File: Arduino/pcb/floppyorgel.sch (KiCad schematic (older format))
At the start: 31 parts, among them J1 Floppy-Bus, J2 Floppy-Bus, J3 FTDI, J4 Buck-Converter-5V, J5 MAX485 Socket, J6 Buck-Converter-12V, J7 IBM_PC_Floppy_IDC, J8 Power Select, J9 Floppy-Power, SW1 Bus Address Select, SW2 Reset Button, U1 ATMEGA328P-AU, U2 74HC595, Y1 20 Mhz Crystal

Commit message: floppyorgel.sch: add bypass caps
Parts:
- added C? (x4): 100nF, symbol Device:C
- added C?: 1500uF, symbol Device:CP
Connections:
- net labels added: LATCH_ADDR, LATCH_LED
- wire segments 169 -> 182
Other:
- note added: "Bypass"
- moved on the sheet: D?, R?, SW1, U2, U?

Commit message: floppyorgel.sch: add hierachical sheets
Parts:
- gave numbers to parts that had none: 22

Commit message: floppyorgel.sch: reduce ERC errors
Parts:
- added R9: 4K7, symbol Device:R
- renumbered J3 to J1, J1 to J2, J4 to J3, J5 to J4, J2 to J5, J8 to J7, J9 to J8, J7 to J9, R9 to R10, R10 to R11, R11 to R12, R12 to R13, SW2 to SW1, SW1 to SW2
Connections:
- net labels removed: +24V, nLATCH
- wire segments 182 -> 185
- no-connect marks 24 -> 35

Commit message: pcb: continue wiring / move parts to hierachival sheets
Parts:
- removed C1, C3, C4, C5, C6: 100nF, symbol Device:C
- removed C2: 1500uF, symbol Device:CP
- removed C7, C8: 22pF, symbol Device:C
- removed D1: LED_RGB, symbol Device:LED_RGB
- removed J1: FTDI, Connector_PinHeader_2.54mm:PinHeader_1x06_P2.54mm_Vertical, symbol ftdi:FTDI
- removed J2, J5: Floppy-Bus, shrouded:Shrouded_Header_2x05_Pitch2.54mm, symbol floppy-bus-connector:Floppy-Bus
- removed J3: Buck-Converter-5V, Connector_PinHeader_2.54mm:PinHeader_1x06_P2.54mm_Vertical, symbol buck-converter:Buck-Converter
- removed J4: MAX485 Socket, Housings_DIP:DIP-8_W7.62mm, symbol Interface_UART:MAX485E
- removed J6: Buck-Converter-12V, Connector_PinHeader_2.54mm:PinHeader_1x06_P2.54mm_Vertical, symbol buck-converter:Buck-Converter
- removed J7: Power Select, Pin_Headers:Pin_Header_Straight_1x02_Pitch2.54mm, symbol Connector:Conn_01x03_Male
- removed J8: Floppy-Power, floppy_power:Floppy_Power_1x04_Pitch2.54mm, symbol floppy-power:Floppy-Power
- removed J9: IBM_PC_Floppy_IDC, Connector_PinHeader_2.54mm:PinHeader_2x17_P2.54mm_Horizontal, symbol ibm_pc_floppy_idc:IBM_PC_Floppy_IDC
- removed R1: 10K, symbol Device:R
- removed R10, R11, R12, R13, R2, R3, R4, R5, R6, R7, R8, R9: 4K7, symbol Device:R
- removed SW1: Reset Button, Buttons_Switches_THT:SW_PUSH_6mm, symbol floppyorgel-rescue:SW_Push_Dual-RESCUE-floppyorgel
- removed SW2: Bus Address Select, Buttons_Switches_THT:SW_DIP_x6_W7.62mm_Slide, symbol floppyorgel-rescue:SW_DIP_x06-switches
- removed U1: ATMEGA328P-AU, Housings_QFP:TQFP-32_7x7mm_Pitch0.8mm, symbol floppyorgel-rescue:ATMEGA328P-AU-atmel
- removed U2: 74HC595, SMD_Packages:SO-16-N, symbol floppyorgel-rescue:74HC595-74xx
- removed U3: 4021, symbol 4xxx_IEEE:4021
- removed Y1: 20 Mhz Crystal, Crystals:Crystal_HC49-4H_Vertical, symbol floppyorgel-rescue:Crystal-device
- added J1: VCC_Power_Select, symbol vcc_power_select:VCC_Power_Select
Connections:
- net labels added: 12V_BUS, 5V_BUS, 5V_ISP
- net labels removed: BUS_POWER, BUS_RX, BUS_TX, DIRECTION, DRIVE_SELECT, GND, LATCH_ADDR, LATCH_LED, MISO, MOSI, RESET, SCK, STEP, TRK00, VCC_BUS, VCC_ISP
- wire segments 185 -> 24
- no-connect marks 35 -> 0
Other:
- note removed: "Bypass"
- note removed: "Output to next module"

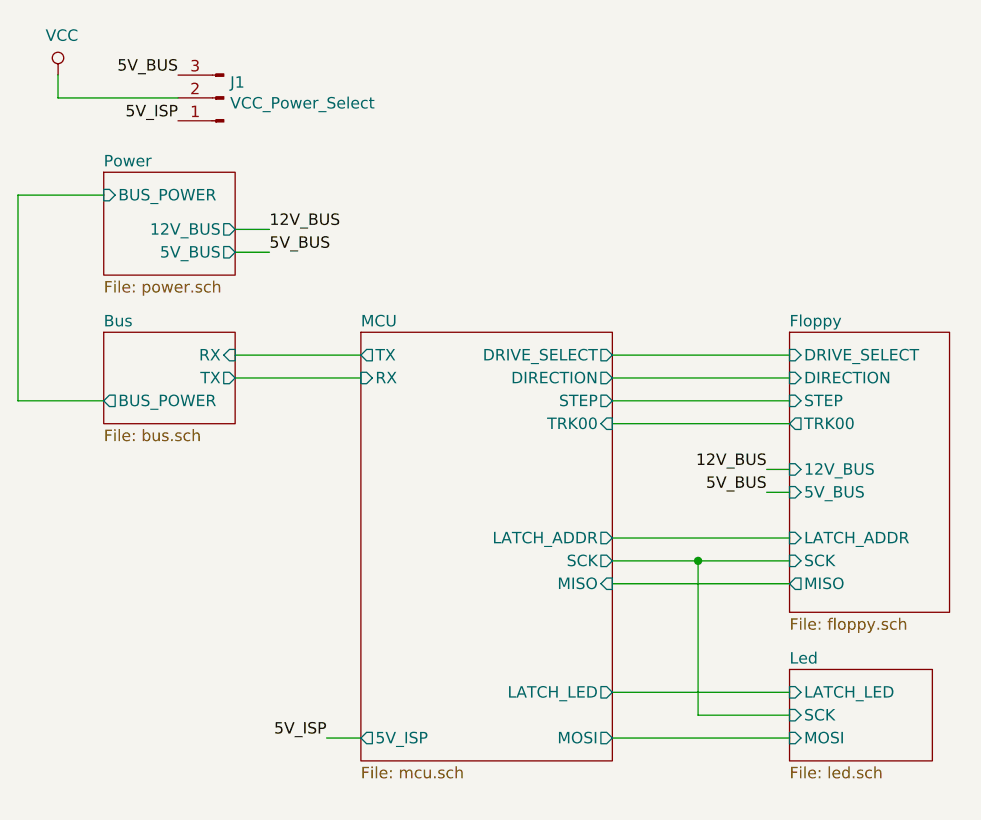
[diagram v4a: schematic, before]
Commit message: pcb: finish wiring / use ws2812 under chip led
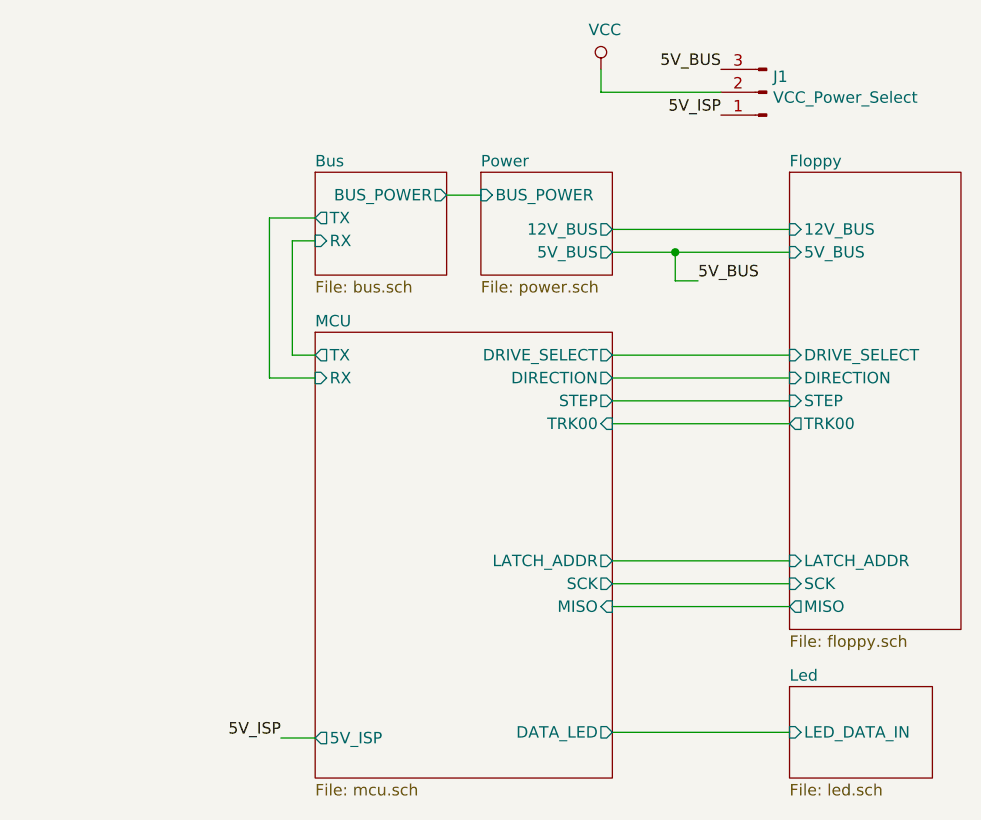
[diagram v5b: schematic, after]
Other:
- moved on the sheet: J1
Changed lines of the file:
@@
 $EndDescr
 $Sheet
-S 5800 3475 700  1225
+S 3725 2775 575  450
+U 5CD1E0A5
+F0 "Bus" 50
+F1 "bus.sch" 50
+F2 "BUS_POWER" O R 4300 2875 50
+F3 "TX" O L 3725 2975 50
+F4 "RX" I L 3725 3075 50
+$EndSheet
+$Sheet
+S 4450 2775 575  450
+U 5CD31258
+F0 "Power" 50
+F1 "power.sch" 50
+F2 "BUS_POWER" I L 4450 2875 50
+F3 "12V_BUS" O R 5025 3025 50
+F4 "5V_BUS" O R 5025 3125 50
+$EndSheet
+Wire Wire Line
+	5025 3875 5800 3875
+Wire Wire Line
+	5800 3775 5025 3775
+$Comp
+L power:VCC #PWR01
+U 1 1 5D10B089
+P 4975 2325
+AR Path="/5D10B089" Ref="#PWR01"  Part="1"
+AR Path="/5CD31258/5D10B089" Ref="#PWR?"  Part="1"
+F 0 "#PWR01" H 4975 2175 50  0001 C CNN
+F 1 "VCC" H 4992 2498 50  0000 C CNN
+F 2 "" H 4975 2325 50  0001 C CNN
+F 3 "" H 4975 2325 50  0001 C CNN
+	1    4975 2325
+	1    0    0    -1
+$EndComp
+Wire Wire Line
+	4975 2325 4975 2425
+Wire Wire Line
+	4975 2425 5500 2425
+$Comp
+L vcc_power_select:VCC_Power_Select J1
+U 1 1 5D19C0BF
+P 5700 2425
+F 0 "J1" H 5672 2357 50  0000 R CNN
+F 1 "VCC_Power_Select" H 5672 2448 50  0000 R CNN
+F 2 "" H 5700 2425 50  0001 C CNN
+F 3 "~" H 5700 2425 50  0001 C CNN
+	1    5700 2425
+	-1   0    0    1
+$EndComp
+Wire Wire Line
+	5800 4675 5025 4675
+Wire Wire Line
+	5025 4475 5800 4475
+Wire Wire Line
+	3625 3575 3725 3575
+Wire Wire Line
+	3725 3675 3525 3675
+Wire Wire Line
+	4300 2875 4450 2875
+Wire Wire Line
+	3725 3075 3625 3075
+Wire Wire Line
+	3625 3075 3625 3575
+Wire Wire Line
+	3525 2975 3725 2975
+Wire Wire Line
+	3525 2975 3525 3675
+Wire Wire Line
+	5025 3025 5800 3025
+Text Label 5500 2525 2    50   ~ 0
+5V_ISP
+Wire Wire Line
+	3575 5250 3725 5250
+Text Label 3575 5250 2    50   ~ 0
+5V_ISP
+Wire Wire Line
+	5025 3575 5800 3575
+Wire Wire Line
+	5025 3675 5800 3675
+$Sheet
+S 5800 2775 750  2000
 U 5CD0EE48
 F0 "Floppy" 50
@@
 F4 "TRK00" O L 5800 3875 50
 F5 "STEP" I L 5800 3775 50
-F6 "5V_BUS" I L 5800 4175 50
-F7 "12V_BUS" I L 5800 4075 50
-F8 "LATCH_ADDR" I L 5800 4375 50
-F9 "SCK" I L 5800 4475 50
-F10 "MISO" O L 5800 4575 50
+F6 "5V_BUS" I L 5800 3125 50
+F7 "12V_BUS" I L 5800 3025 50
+F8 "LATCH_ADDR" I L 5800 4475 50
+F9 "SCK" I L 5800 4575 50
+F10 "MISO" O L 5800 4675 50
 $EndSheet
 $Sheet
-S 2800 3475 575  400
-U 5CD1E0A5
-F0 "Bus" 50
-F1 "bus.sch" 50
-F2 "BUS_POWER" O L 2800 3775 50
-F3 "TX" O R 3375 3675 50
-F4 "RX" I R 3375 3575 50
-$EndSheet
-$Sheet
-S 2800 2775 575  450
-U 5CD31258
-F0 "Power" 50
-F1 "power.sch" 50
-F2 "BUS_POWER" I L 2800 2875 50
-F3 "12V_BUS" O R 3375 3025 50
-F4 "5V_BUS" O R 3375 3125 50
-$EndSheet
-$Sheet
-S 5800 4950 625  400
-U 5CD3FBA6
-F0 "Led" 50
-F1 "led.sch" 50
-F2 "MOSI" I L 5800 5250 50
-F3 "SCK" I L 5800 5150 50
-F4 "LATCH_LED" I L 5800 5050 50
-$EndSheet
-Wire Wire Line
-	3775 5250 3925 5250
-Wire Wire Line
-	5025 3575 5800 3575
-Wire Wire Line
-	5025 3875 5800 3875
-Wire Wire Line
-	5025 3675 5800 3675
-Wire Wire Line
-	5800 3775 5025 3775
-$Sheet
-S 3925 3475 1100 1875
+S 3725 3475 1300 1950
 U 5CCFEC3E
 F0 "MCU" 50
@@
 F3 "DIRECTION" O R 5025 3675 50
 F4 "STEP" O R 5025 3775 50
-F5 "MOSI" O R 5025 5250 50
-F6 "MISO" I R 5025 4575 50
-F7 "SCK" O R 5025 4475 50
-F8 "TRK00" I R 5025 3875 50
-F9 "LATCH_ADDR" O R 5025 4375 50
-F10 "LATCH_LED" O R 5025 5050 50
-F11 "5V_ISP" O L 3925 5250 50
-F12 "RX" I L 3925 3675 50
-F13 "TX" O L 3925 3575 50
+F5 "MISO" I R 5025 4675 50
+F6 "SCK" O R 5025 4575 50
+F7 "TRK00" I R 5025 3875 50
+F8 "LATCH_ADDR" O R 5025 4475 50
+F9 "5V_ISP" O L 3725 5250 50
+F10 "RX" I L 3725 3675 50
+F11 "TX" O L 3725 3575 50
+F12 "DATA_LED" O R 5025 5225 50
+$EndSheet
+Text Label 5500 2325 2    50   ~ 0
+5V_BUS
+Wire Wire Line
+	5025 3125 5300 3125
+Text Label 5400 3250 0    50   ~ 0
+5V_BUS
+Wire Wire Line
+	5400 3250 5300 3250
+Wire Wire Line
+	5300 3250 5300 3125
+Connection ~ 5300 3125
+Wire Wire Line
+	5300 3125 5800 3125
+$Sheet
+S 5800 5025 625  400
+U 5CD3FBA6
+F0 "Led" 50
+F1 "led.sch" 50
+F2 "LED_DATA_IN" I L 5800 5225 50
 $EndSheet
 Wire Wire Line
-	2425 3775 2800 3775
+	5025 4575 5800 4575
 Wire Wire Line
-	3375 3025 3525 3025
-Wire Wire Line
-	3375 3125 3525 3125
-Text Label 3525 3125 0    50   ~ 0
-5V_BUS
-Text Label 3525 3025 0    50   ~ 0
-12V_BUS
-Text Label 3775 5250 2    50   ~ 0
-5V_ISP
-Text Label 5700 4075 2    50   ~ 0
-12V_BUS
-Text Label 5700 4175 2    50   ~ 0
-5V_BUS
-Wire Wire Line
-	5700 4075 5800 4075
-Wire Wire Line
-	5700 4175 5800 4175
-Wire Wire Line
-	2800 2875 2425 2875
-Wire Wire Line
-	2425 2875 2425 3775
-$Comp
-L power:VCC #PWR01
-U 1 1 5D10B089
-P 2600 2350
-AR Path="/5D10B089" Ref="#PWR01"  Part="1"
-AR Path="/5CD31258/5D10B089" Ref="#PWR?"  Part="1"
-F 0 "#PWR01" H 2600 2200 50  0001 C CNN
-F 1 "VCC" H 2617 2523 50  0000 C CNN
-F 2 "" H 2600 2350 50  0001 C CNN
-F 3 "" H 2600 2350 50  0001 C CNN
-	1    2600 2350
-	1    0    0    -1
-$EndComp
-Wire Wire Line
-	2600 2350 2600 2450
-Wire Wire Line
-	2600 2450 3125 2450
-Text Label 3125 2550 2    50   ~ 0
-5V_ISP
-Text Label 3125 2350 2    50   ~ 0
-5V_BUS
-$Comp
-L vcc_power_select:VCC_Power_Select J1
-U 1 1 5D19C0BF
-P 3325 2450
-F 0 "J1" H 3297 2382 50  0000 R CNN
-F 1 "VCC_Power_Select" H 3297 2473 50  0000 R CNN
-F 2 "" H 3325 2450 50  0001 C CNN
-F 3 "~" H 3325 2450 50  0001 C CNN
-	1    3325 2450
-	-1   0    0    1
-$EndComp
-Wire Wire Line
-	5800 5050 5025 5050
-Wire Wire Line
-	5800 4375 5025 4375
-Wire Wire Line
-	5800 4575 5025 4575
-Wire Wire Line
-	5025 4475 5400 4475
-Wire Wire Line
-	5800 5250 5025 5250
-Wire Wire Line
-	5800 5150 5400 5150
-Wire Wire Line
-	5400 5150 5400 4475
-Connection ~ 5400 4475
-Wire Wire Line
-	5400 4475 5800 4475
-Wire Wire Line
-	3375 3575 3925 3575
-Wire Wire Line
-	3375 3675 3925 3675
+	5025 5225 5800 5225
 $EndSCHEMATC

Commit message: pcb: assign footprints
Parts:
- J1: footprint (none) -> Connector_PinHeader_2.54mm:PinHeader_1x03_P2.54mm_Vertical
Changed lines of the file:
@@
 F 0 "J1" H 5672 2357 50  0000 R CNN
 F 1 "VCC_Power_Select" H 5672 2448 50  0000 R CNN
-F 2 "" H 5700 2425 50  0001 C CNN
+F 2 "Connector_PinHeader_2.54mm:PinHeader_1x03_P2.54mm_Vertical" H 5700 2425 50  0001 C CNN
 F 3 "~" H 5700 2425 50  0001 C CNN
 	1    5700 2425

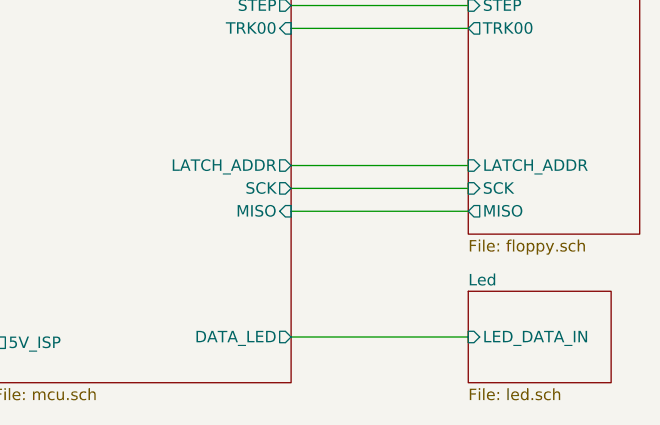
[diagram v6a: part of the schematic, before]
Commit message: pcb: continue placement + add some info on silk
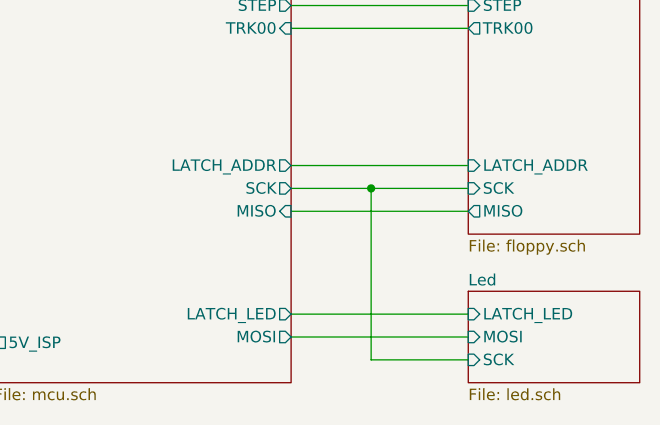
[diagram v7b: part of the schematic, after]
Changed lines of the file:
@@
 F10 "RX" I L 3725 3675 50
 F11 "TX" O L 3725 3575 50
-F12 "DATA_LED" O R 5025 5225 50
+F12 "LATCH_LED" O R 5025 5125 50
+F13 "MOSI" O R 5025 5225 50
 $EndSheet
 Text Label 5500 2325 2    50   ~ 0
@@
 	5300 3125 5800 3125
 $Sheet
-S 5800 5025 625  400
+S 5800 5025 750  400
 U 5CD3FBA6
 F0 "Led" 50
 F1 "led.sch" 50
-F2 "LED_DATA_IN" I L 5800 5225 50
+F2 "MOSI" I L 5800 5225 50
+F3 "SCK" I L 5800 5325 50
+F4 "LATCH_LED" I L 5800 5125 50
 $EndSheet
 Wire Wire Line
-	5025 4575 5800 4575
+	5025 4575 5375 4575
+Wire Wire Line
+	5025 5125 5800 5125
+Connection ~ 5375 4575
+Wire Wire Line
+	5375 4575 5800 4575
+Wire Wire Line
+	5800 5325 5375 5325
+Wire Wire Line
+	5375 4575 5375 5325
 Wire Wire Line
 	5025 5225 5800 5225

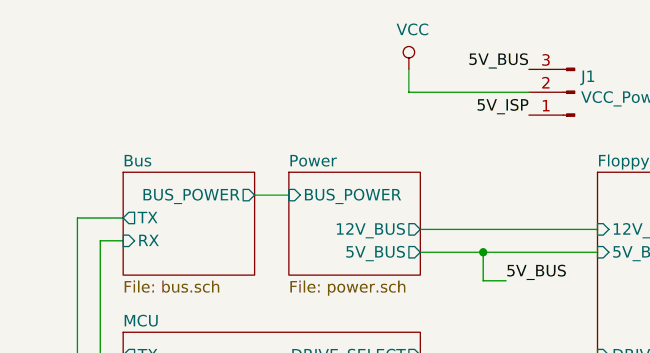
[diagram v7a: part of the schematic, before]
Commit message: pcb: fix logo library
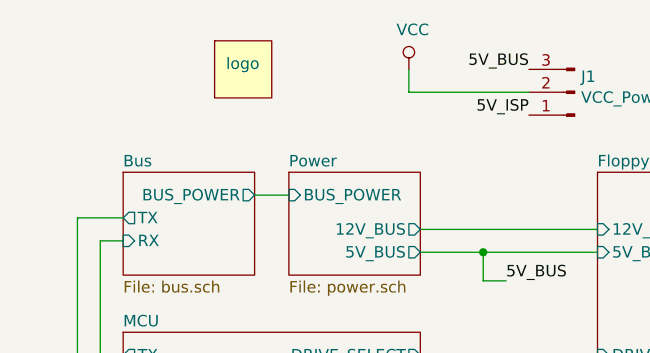
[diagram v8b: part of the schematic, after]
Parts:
- added L1: logo, logo:logo, symbol logo:logo
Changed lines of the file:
@@
 EESchema Schematic File Version 4
-LIBS:floppyorgel-cache
 EELAYER 29 0
 EELAYER END
@@
 Wire Wire Line
 	5025 5225 5800 5225
+$Comp
+L logo:logo L1
+U 1 1 5CDF6702
+P 4250 2325
+F 0 "L1" H 4250 2400 50  0001 C CNN
+F 1 "logo" H 4175 2350 50  0000 L CNN
+F 2 "logo:logo" H 4250 2325 50  0001 C CNN
+F 3 "" H 4250 2325 50  0001 C CNN
+	1    4250 2325
+	1    0    0    -1
+$EndComp
 $EndSCHEMATC
